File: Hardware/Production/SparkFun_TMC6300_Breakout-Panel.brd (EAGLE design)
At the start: 114 x 117.9 mm, 1626 parts, among them U1 TMC6300, U10 TMC6300, U11 TMC6300, U12 TMC6300, U13 TMC6300, U14 TMC6300, U15 TMC6300, U16 TMC6300, U17 TMC6300, U18 TMC6300, U19 TMC6300, U2 TMC6300, U20 TMC6300, U21 TMC6300, U22 TMC6300, U23 TMC6300, U24 TMC6300, U25 TMC6300, U26 TMC6300, U27 TMC6300, U28 TMC6300, U29 TMC6300, U3 TMC6300, U30 TMC6300, U4 TMC6300, U5 TMC6300, U6 TMC6300, U7 TMC6300, U8 TMC6300, U9 TMC6300

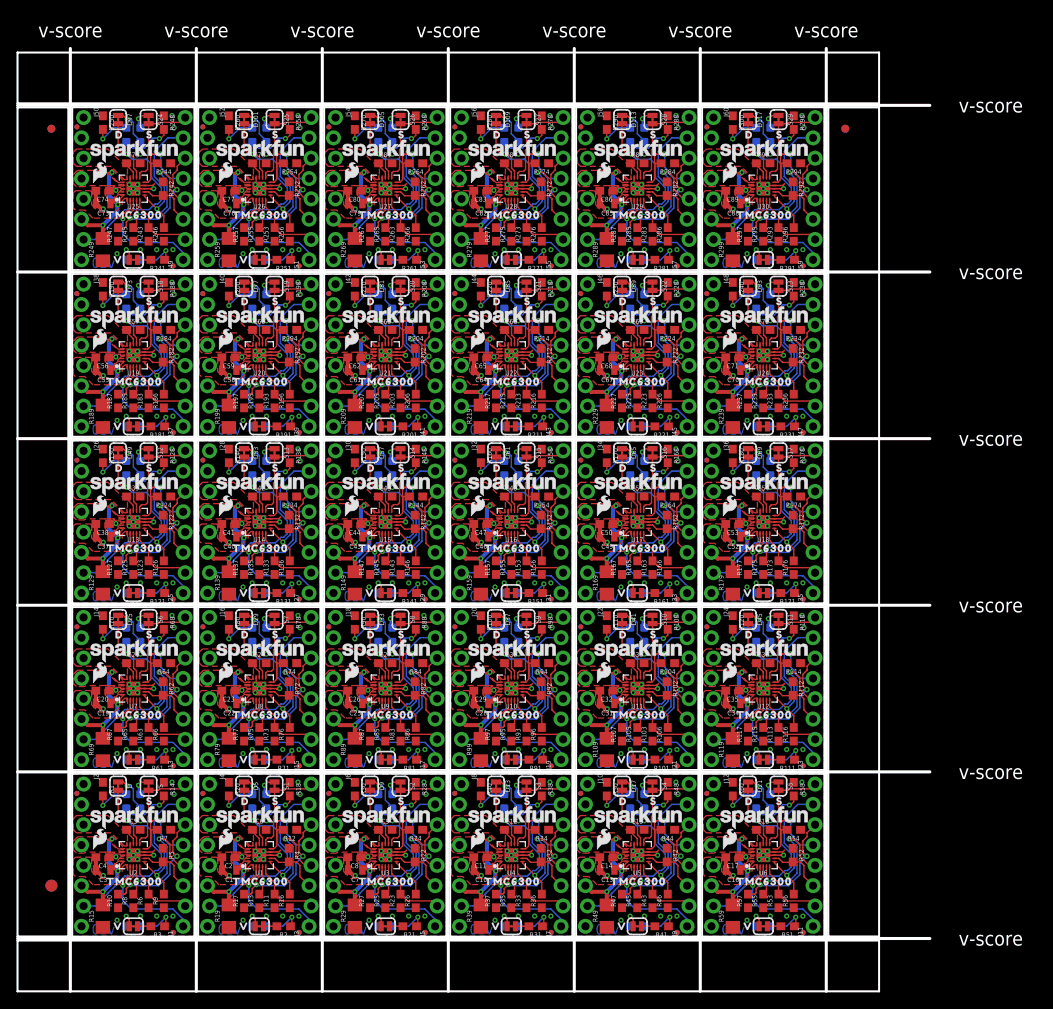
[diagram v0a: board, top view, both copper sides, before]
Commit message: Updated production files
Re generated panelized files for ordering from design review changes
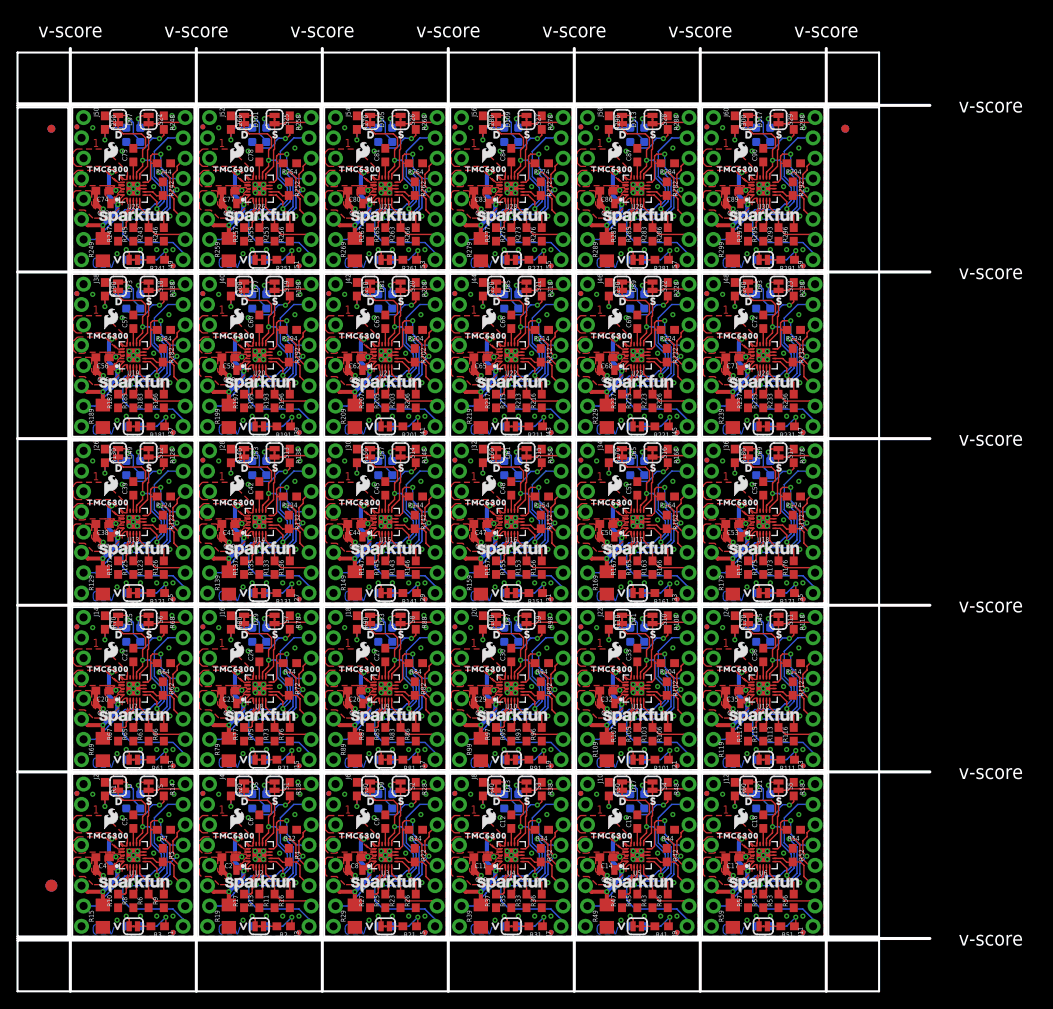
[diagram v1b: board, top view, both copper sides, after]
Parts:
- LOGO1, LOGO10, LOGO13, LOGO16, LOGO19, LOGO22, LOGO25, LOGO28, LOGO3, LOGO31, LOGO34, LOGO37, LOGO40, LOGO43, LOGO46, LOGO49, LOGO52, LOGO55, LOGO58, LOGO61, LOGO64, LOGO67, LOGO7, LOGO70, LOGO73, LOGO76, LOGO79, LOGO82, LOGO85, LOGO88: value SFE_LOGO_NAME.1_INCH -> SFE_LOGO_NAME.08_INCH; device SparkFun-Aesthetics:SFE_LOGO_NAME_.1 -> SparkFun-Aesthetics:SFE_LOGO_NAME_.08
- U$100, U$125, U$150, U$175, U$200, U$225, U$250, U$275, U$300, U$325, U$350, U$375, U$400, U$425, U$450, U$475, U$50, U$500, U$525, U$550, U$575, U$600, U$625, U$650, U$675, U$700, U$725, U$75, U$750: device output:#DIAG#0 -> output:TMC630063003454
- U$104, U$129, U$154, U$179, U$204, U$229, U$254, U$279, U$304, U$329, U$354, U$379, U$404, U$429, U$454, U$479, U$504, U$529, U$54, U$554, U$579, U$604, U$629, U$654, U$679, U$704, U$729, U$79: device output:TMC63000 -> output:D0
- U$105, U$130, U$155, U$180, U$205, U$230, U$255, U$280, U$305, U$330, U$355, U$380, U$405, U$430, U$455, U$480, U$505, U$530, U$55, U$555, U$580, U$605, U$630, U$655, U$680, U$705, U$730, U$80: device output:D0 -> output:V2
- U$106, U$131, U$156, U$181, U$206, U$231, U$256, U$281, U$306, U$331, U$356, U$381, U$406, U$431, U$456, U$481, U$506, U$531, U$556, U$56, U$581, U$606, U$631, U$656, U$681, U$706, U$731, U$81: device output:V2 -> output:S1
- U$107, U$132, U$157, U$182, U$207, U$232, U$257, U$282, U$307, U$332, U$357, U$382, U$407, U$432, U$457, U$482, U$507, U$532, U$557, U$57, U$582, U$607, U$632, U$657, U$682, U$707, U$732, U$82: device output:S1 -> output:D0
- U$108, U$133, U$158, U$183, U$208, U$233, U$258, U$283, U$308, U$333, U$358, U$383, U$408, U$433, U$458, U$483, U$508, U$533, U$558, U$58, U$583, U$608, U$633, U$658, U$683, U$708, U$733, U$83: device output:D0 -> output:S1
- U$109, U$134, U$159, U$184, U$209, U$234, U$259, U$284, U$29, U$309, U$334, U$359, U$384, U$409, U$434, U$459, U$484, U$509, U$534, U$559, U$584, U$59, U$609, U$634, U$659, U$684, U$709, U$734, U$84: device output:S1 -> output:V2
- U$110, U$135, U$160, U$185, U$210, U$235, U$260, U$285, U$310, U$335, U$35, U$360, U$385, U$410, U$435, U$460, U$485, U$510, U$535, U$560, U$585, U$60, U$610, U$635, U$660, U$685, U$710, U$735, U$85: device output:V2 -> output:63001
- U$111, U$136, U$161, U$186, U$211, U$236, U$261, U$286, U$311, U$336, U$36, U$361, U$386, U$411, U$436, U$461, U$486, U$511, U$536, U$561, U$586, U$61, U$611, U$636, U$661, U$686, U$711, U$736, U$86: device output:63001 -> output:TMC0
- U$112, U$137, U$162, U$187, U$212, U$237, U$262, U$287, U$312, U$337, U$362, U$37, U$387, U$412, U$437, U$462, U$487, U$512, U$537, U$562, U$587, U$612, U$62, U$637, U$662, U$687, U$712, U$737, U$87: device output:TMC0 -> output:#VIN#0
- U$113, U$138, U$163, U$188, U$213, U$238, U$263, U$288, U$313, U$338, U$363, U$38, U$388, U$413, U$438, U$463, U$488, U$513, U$538, U$563, U$588, U$613, U$63, U$638, U$663, U$688, U$713, U$738, U$88: device output:#VIN#0 -> output:#GND#1
- U$114, U$139, U$164, U$189, U$214, U$239, U$264, U$289, U$314, U$339, U$364, U$389, U$39, U$414, U$439, U$464, U$489, U$514, U$539, U$564, U$589, U$614, U$639, U$64, U$664, U$689, U$714, U$739, U$89: device output:#GND#1 -> output:#U#6
- U$115, U$140, U$165, U$190, U$215, U$240, U$265, U$290, U$315, U$340, U$365, U$390, U$40, U$415, U$440, U$465, U$490, U$515, U$540, U$565, U$590, U$615, U$640, U$65, U$665, U$690, U$715, U$740, U$90: device output:#U#6 -> output:#UH#5
- U$116, U$141, U$166, U$191, U$216, U$241, U$266, U$291, U$316, U$341, U$366, U$391, U$41, U$416, U$441, U$466, U$491, U$516, U$541, U$566, U$591, U$616, U$641, U$66, U$666, U$691, U$716, U$741, U$91: device output:#UH#5 -> output:#UL#4
- U$117, U$142, U$167, U$192, U$217, U$242, U$267, U$292, U$317, U$342, U$367, U$392, U$417, U$42, U$442, U$467, U$492, U$517, U$542, U$567, U$592, U$617, U$642, U$667, U$67, U$692, U$717, U$742, U$92: device output:#UL#4 -> output:#V#7
- U$118, U$143, U$168, U$193, U$218, U$243, U$268, U$293, U$318, U$343, U$368, U$393, U$418, U$43, U$443, U$468, U$493, U$518, U$543, U$568, U$593, U$618, U$643, U$668, U$68, U$693, U$718, U$743, U$93: device output:#V#7 -> output:#VH#2
- U$119, U$144, U$169, U$194, U$219, U$244, U$269, U$294, U$319, U$344, U$369, U$394, U$419, U$44, U$444, U$469, U$494, U$519, U$544, U$569, U$594, U$619, U$644, U$669, U$69, U$694, U$719, U$744, U$94: device output:#VH#2 -> output:#VL#3
- U$120, U$145, U$170, U$195, U$220, U$245, U$270, U$295, U$320, U$345, U$370, U$395, U$420, U$445, U$45, U$470, U$495, U$520, U$545, U$570, U$595, U$620, U$645, U$670, U$695, U$70, U$720, U$745, U$95: device output:#VL#3 -> output:#W#8
- U$121, U$146, U$171, U$196, U$221, U$246, U$271, U$296, U$321, U$346, U$371, U$396, U$421, U$446, U$46, U$471, U$496, U$521, U$546, U$571, U$596, U$621, U$646, U$671, U$696, U$71, U$721, U$746, U$96: device output:#W#8 -> output:#WH#1
- U$122, U$147, U$172, U$197, U$222, U$247, U$272, U$297, U$322, U$347, U$372, U$397, U$422, U$447, U$47, U$472, U$497, U$522, U$547, U$572, U$597, U$622, U$647, U$672, U$697, U$72, U$722, U$747, U$97: device output:#WH#1 -> output:#WL#0
- U$123, U$148, U$173, U$198, U$223, U$248, U$273, U$298, U$323, U$348, U$373, U$398, U$423, U$448, U$473, U$48, U$498, U$523, U$548, U$573, U$598, U$623, U$648, U$673, U$698, U$723, U$73, U$748, U$98: device output:#WL#0 -> output:#SEN#0
- U$124, U$149, U$174, U$199, U$224, U$249, U$274, U$299, U$324, U$349, U$374, U$399, U$424, U$449, U$474, U$49, U$499, U$524, U$549, U$574, U$599, U$624, U$649, U$674, U$699, U$724, U$74, U$749, U$99: device output:#SEN#0 -> output:#DIAG#0
- U$17: device output:TMC63000 -> output:S1
- U$4: device output:#GND#1 -> output:TMC630063003454
- U$5: device output:#VCP#0 -> output:#GND#1
- U$6: device output:#VIO#1 -> output:#VCP#0
- U$7: device output:TMC63000 -> output:#VIO#1
- moved U$17 20.7 mm to (25.3, 17.8), flipped to the bottom
- moved U$6 17.8 mm to (26.9, 1.27)
- moved U$463 17.8 mm to (3.81, 63.8)
- moved U$488 17.8 mm to (19.6, 63.8)
- moved U$513 17.8 mm to (35.3, 63.8)
- moved U$538 17.8 mm to (51.1, 63.8)
- moved U$563 17.8 mm to (66.8, 63.8)
- moved U$588 17.8 mm to (82.5, 63.8)
- moved U$113 17.8 mm to (66.8, 1.27)
- moved U$138 17.8 mm to (82.5, 1.27)
- moved U$163 17.8 mm to (3.81, 22.1)
- moved U$188 17.8 mm to (19.6, 22.1)
- moved U$213 17.8 mm to (35.3, 22.1)
- moved U$238 17.8 mm to (51.1, 22.1)
- moved U$263 17.8 mm to (66.8, 22.1)
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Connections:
- net DIAG: now also U1.12; no longer U2.12
- net DIAG1: now also U2.12; no longer U1.12
- net GND: now also U1.14, U1.8, U1.9, U1.PAD; no longer U2.14, U2.8, U2.9, U2.PAD
- net GND1: now also U2.14, U2.8, U2.9, U2.PAD; no longer U1.14, U1.8, U1.9, U1.PAD
- net N$6: now also U1.13; no longer U2.13
- net N$7: now also U2.13; no longer U1.13
- net SENSE: now also U1.16, U1.20; no longer U2.16, U2.20
- net SENSE1: now also U2.16, U2.20; no longer U1.16, U1.20
- net U: now also U1.15; no longer U2.15
- net U1: now also U2.15; no longer U1.15
- net UH: now also U1.3; no longer U2.3
- net UH1: now also U2.3; no longer U1.3
- net UL: now also U1.6; no longer U2.6
- net UL1: now also U2.6; no longer U1.6
- net V: now also U1.17; no longer U2.17
- net V1: now also U2.17; no longer U1.17
- net VCP: now also U1.2; no longer U2.2
- net VCP1: now also U2.2; no longer U1.2
- net VH: now also U1.4; no longer U2.4
- net VH1: now also U2.4; no longer U1.4
- net VIN: now also U1.18; no longer U2.18
- net VIN1: now also U2.18; no longer U1.18
- net VIO/!STDBY!: now also U1.11; no longer U2.11
- net VIO/!STDBY!1: now also U2.11; no longer U1.11
- net VL: now also U1.10; no longer U2.10
- net VL1: now also U2.10; no longer U1.10
- net W: now also U1.1; no longer U2.1
- net W1: now also U2.1; no longer U1.1
- net WH: now also U1.5; no longer U2.5
- net WH1: now also U2.5; no longer U1.5
- net WL: now also U1.7; no longer U2.7
- net WL1: now also U2.7; no longer U1.7
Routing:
- net GND14: track 8.12 -> 4.16 mm, vias 14 -> 17
- net GND2: track 8.12 -> 4.16 mm, vias 14 -> 17
- net GND26: track 8.12 -> 4.16 mm, vias 14 -> 17
- net GND12: track 8.12 -> 4.16 mm, vias 14 -> 17
- net GND8: track 8.12 -> 4.16 mm, vias 14 -> 17
- net GND13: track 8.12 -> 4.16 mm, vias 14 -> 17
- net GND20: track 8.12 -> 4.16 mm, vias 14 -> 17
- net GND: track 8.12 -> 4.16 mm, vias 14 -> 17
- net GND1: track 8.12 -> 4.16 mm, vias 14 -> 17
- net GND16: track 8.12 -> 4.16 mm, vias 14 -> 17
- net GND7: track 8.12 -> 4.16 mm, vias 14 -> 17
- net GND6: track 8.12 -> 4.16 mm, vias 14 -> 17
- net GND25: track 8.12 -> 4.16 mm, vias 14 -> 17
- net GND24: track 8.12 -> 4.16 mm, vias 14 -> 17
- net GND4: track 8.12 -> 4.16 mm, vias 14 -> 17
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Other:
- board text added: "1"
- board text added: "2"
- board text added: "3"
- board text added: "4"

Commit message: Final updates before ordering
Adjusted GND traces from TMC6300 for better connection, added paragraph for Power LED in schematic, updated panelized files for ordering.
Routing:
- net GND8: track 4.16 -> 5.40 mm
- net GND4: track 4.16 -> 5.40 mm
- net GND28: track 4.16 -> 5.40 mm
- net GND26: track 4.16 -> 5.40 mm
- net GND22: track 4.16 -> 5.40 mm
- net GND20: track 4.16 -> 5.40 mm
- net GND2: track 4.16 -> 5.40 mm
- net GND16: track 4.16 -> 5.40 mm
- net GND14: track 4.16 -> 5.40 mm
- net GND10: track 4.16 -> 5.40 mm
- net GND6: track 4.16 -> 5.40 mm
- net GND24: track 4.16 -> 5.40 mm
- net GND18: track 4.16 -> 5.40 mm
- net GND12: track 4.16 -> 5.40 mm
- net GND: track 4.16 -> 5.40 mm
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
